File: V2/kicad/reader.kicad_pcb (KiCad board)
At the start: 2 copper layers, 42.5 x 62 mm, 90 parts, among them SW1 SW_Rezistance, SW2 SW_src, U1 STM32H523CET6, U2 MAX98357AETE+T, U3 MLD-TF PUSH-H18, U4 TCAN1057AVDRQ1, U5 ESD2CAN24-ES, U6 RJ-064-1, U7 MCP16301Hx-xCH, Y1 16MHz

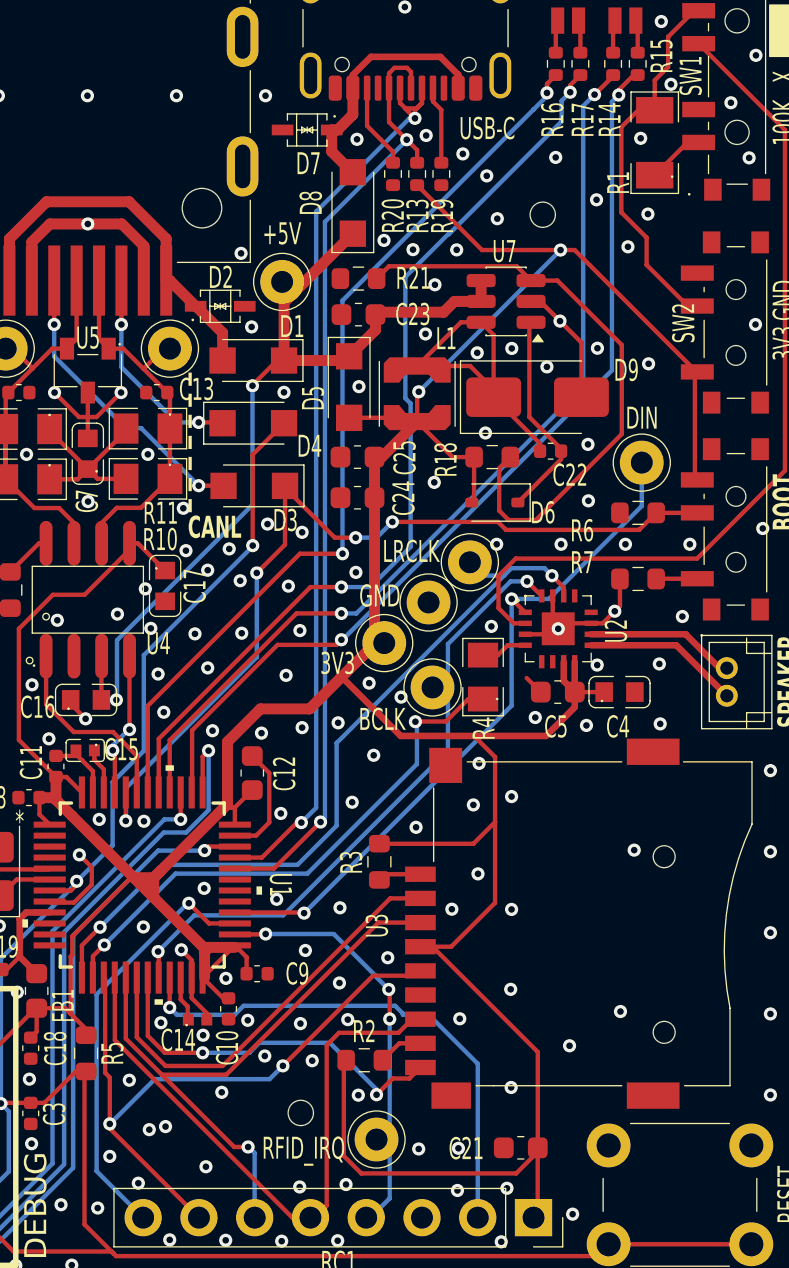
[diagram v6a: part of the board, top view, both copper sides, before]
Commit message: added fiducials
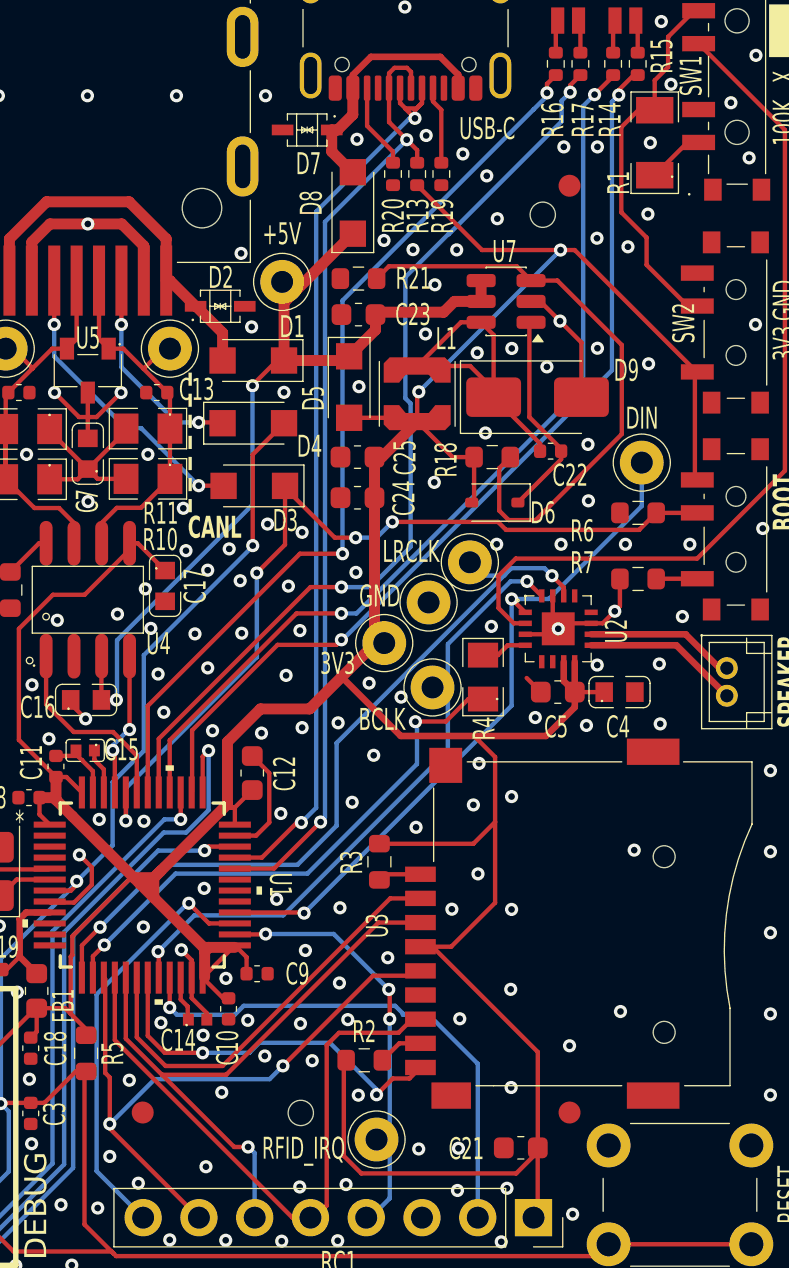
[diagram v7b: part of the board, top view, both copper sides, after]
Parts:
- added REF**: Fiducial_1mm_Mask2mm, Fiducial:Fiducial_1mm_Mask2mm, F.Cu at (164.5, 39.9)
- added REF**: Fiducial_1mm_Mask2mm, Fiducial:Fiducial_1mm_Mask2mm, F.Cu at (164.5, 82.1)
- added REF**: Fiducial_1mm_Mask2mm, Fiducial:Fiducial_1mm_Mask2mm, F.Cu at (145.0, 82.1)
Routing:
- net GND: vias 183 -> 182

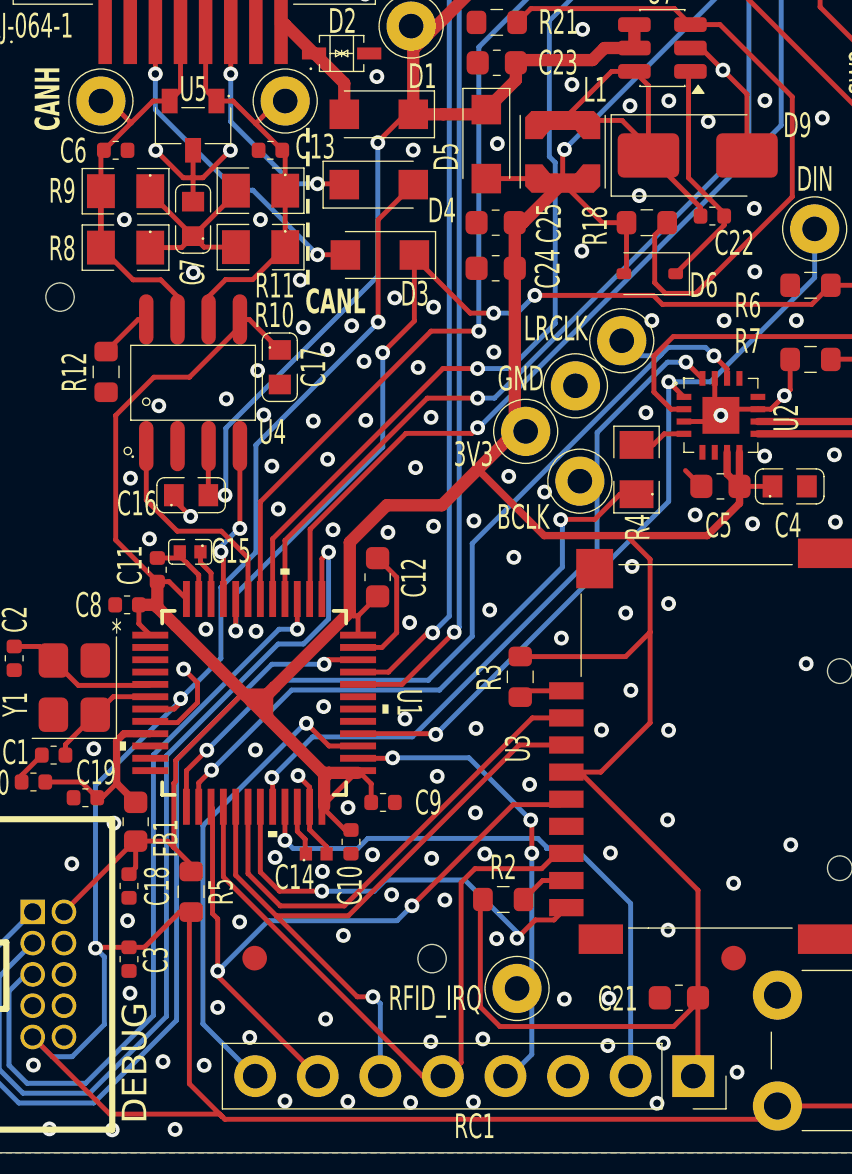
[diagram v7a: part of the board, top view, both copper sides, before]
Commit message: small changes... stm32 pins in cubemx set based on schematic.
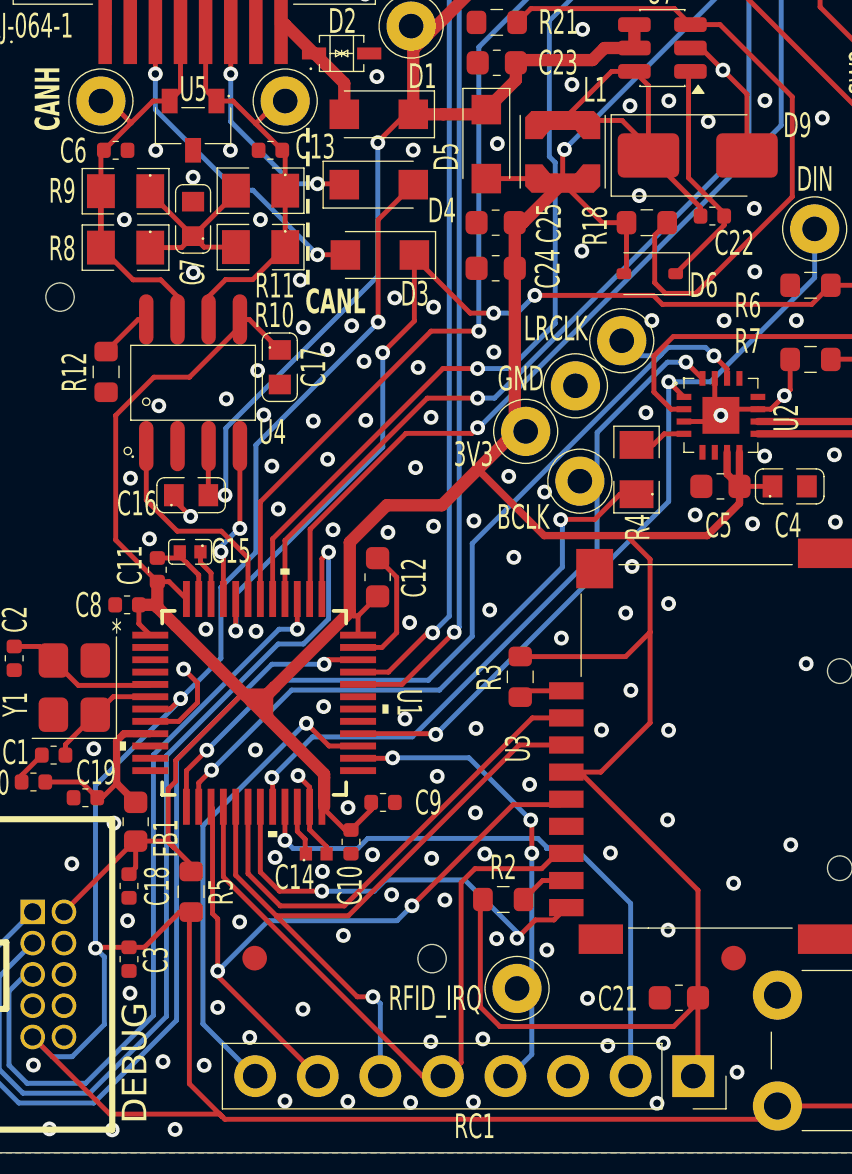
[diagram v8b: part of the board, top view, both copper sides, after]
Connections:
- U1 pad 25: +3.3V -> unconnected-(U1-PB12-Pad25)
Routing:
- net GND: track 43.3 -> 36.3 mm, vias 182 -> 183
- net +3.3V: track 189.8 -> 186.3 mm
